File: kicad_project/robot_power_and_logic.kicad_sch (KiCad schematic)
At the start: 16 parts

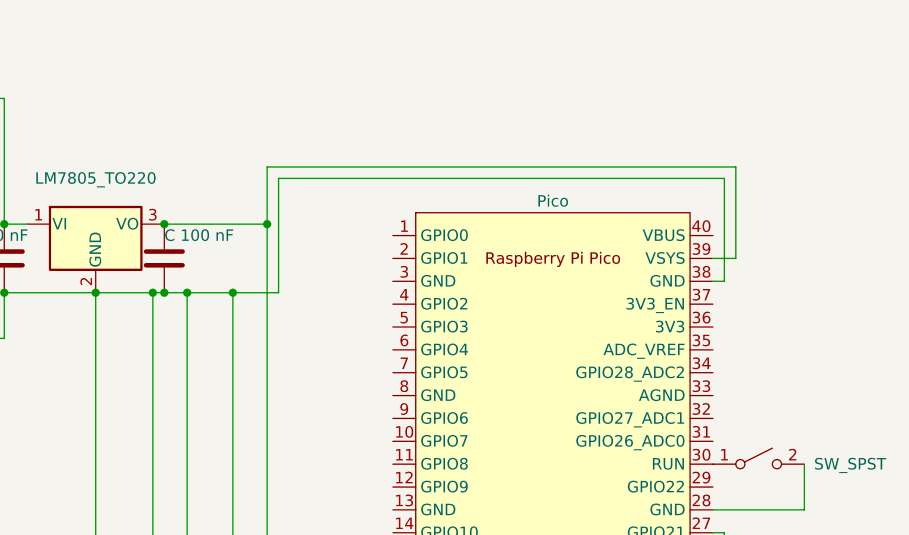
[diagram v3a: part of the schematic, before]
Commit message: Add HC-05 pinout
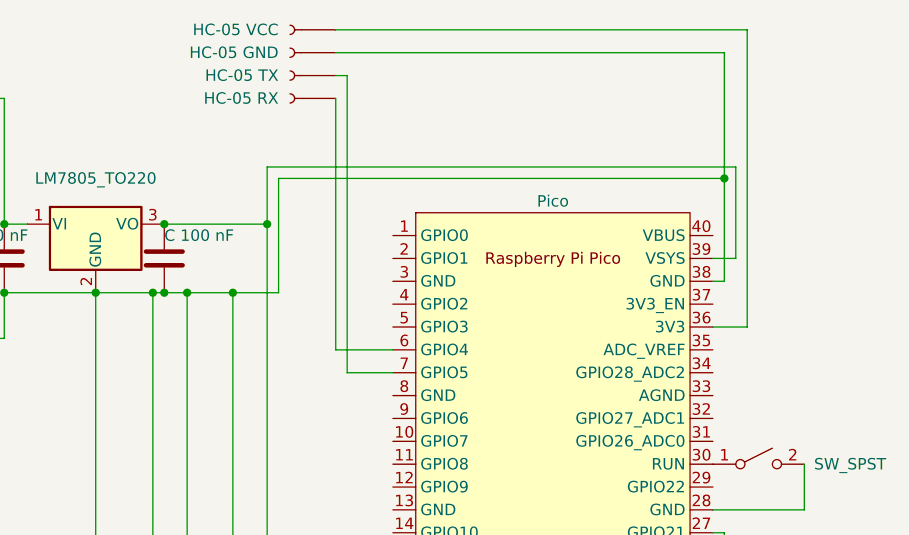
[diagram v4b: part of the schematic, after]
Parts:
- added J?: HC-05 RX, symbol Connector:Conn_01x01_Female
- added J?: HC-05 GND, symbol Connector:Conn_01x01_Female
- added J?: HC-05 VCC, symbol Connector:Conn_01x01_Female
- added J?: HC-05 TX, symbol Connector:Conn_01x01_Female
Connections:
- net at BT?.2 (-), C?.1, C?.1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: now also J?.1 (Pin_1)
- net at U?.36 (3V3): now also J?.1 (Pin_1)
- net at U?.6 (GPIO4): now also J?.1 (Pin_1)
- net at U?.7 (GPIO5): now also J?.1 (Pin_1)
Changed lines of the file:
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@@
   (junction (at 113.03 165.1) (diameter 0) (color 0 0 0 0)
   )
+  (junction (at 139.7 40.64) (diameter 0) (color 0 0 0 0)
+  )
   (junction (at 77.47 45.72) (diameter 0) (color 0 0 0 0)
   )
@@
     (stroke (width 0) (type default) (color 0 0 0 0))
   )
+  (wire (pts (xy 96.52 26.67) (xy 139.7 26.67))
+    (stroke (width 0) (type default) (color 0 0 0 0))
+  )
   (wire (pts (xy 118.11 215.9) (xy 113.03 215.9))
     (stroke (width 0) (type default) (color 0 0 0 0))
@@
     (stroke (width 0) (type default) (color 0 0 0 0))
   )
+  (wire (pts (xy 142.24 57.15) (xy 138.43 57.15))
+    (stroke (width 0) (type default) (color 0 0 0 0))
+  )
   (wire (pts (xy 113.03 215.9) (xy 110.49 215.9))
     (stroke (width 0) (type default) (color 0 0 0 0))
@@
     (stroke (width 0) (type default) (color 0 0 0 0))
   )
+  (wire (pts (xy 139.7 26.67) (xy 139.7 40.64))
+    (stroke (width 0) (type default) (color 0 0 0 0))
+  )
   (wire (pts (xy 59.69 45.72) (xy 62.23 45.72))
     (stroke (width 0) (type default) (color 0 0 0 0))
@@
     (stroke (width 0) (type default) (color 0 0 0 0))
   )
+  (wire (pts (xy 142.24 24.13) (xy 142.24 57.15))
+    (stroke (width 0) (type default) (color 0 0 0 0))
+  )
   (wire (pts (xy 139.7 157.48) (xy 101.6 157.48))
     (stroke (width 0) (type default) (color 0 0 0 0))
@@
     (stroke (width 0) (type default) (color 0 0 0 0))
   )
+  (wire (pts (xy 97.79 29.21) (xy 96.52 29.21))
+    (stroke (width 0) (type default) (color 0 0 0 0))
+  )
   (wire (pts (xy 120.65 215.9) (xy 118.11 215.9))
     (stroke (width 0) (type default) (color 0 0 0 0))
@@
     (stroke (width 0) (type default) (color 0 0 0 0))
   )
+  (wire (pts (xy 97.79 62.23) (xy 97.79 29.21))
+    (stroke (width 0) (type default) (color 0 0 0 0))
+  )
   (wire (pts (xy 110.49 214.63) (xy 110.49 215.9))
     (stroke (width 0) (type default) (color 0 0 0 0))
@@
     (stroke (width 0) (type default) (color 0 0 0 0))
   )
+  (wire (pts (xy 96.52 59.69) (xy 96.52 31.75))
+    (stroke (width 0) (type default) (color 0 0 0 0))
+  )
   (wire (pts (xy 128.27 124.46) (xy 152.4 124.46))
     (stroke (width 0) (type default) (color 0 0 0 0))
@@
     (stroke (width 0) (type default) (color 0 0 0 0))
   )
+  (wire (pts (xy 102.87 62.23) (xy 97.79 62.23))
+    (stroke (width 0) (type default) (color 0 0 0 0))
+  )
   (wire (pts (xy 120.65 214.63) (xy 120.65 215.9))
     (stroke (width 0) (type default) (color 0 0 0 0))
   )
+  (wire (pts (xy 96.52 24.13) (xy 142.24 24.13))
+    (stroke (width 0) (type default) (color 0 0 0 0))
+  )
   (wire (pts (xy 140.97 49.53) (xy 140.97 39.37))
     (stroke (width 0) (type default) (color 0 0 0 0))
@@
   )
   (wire (pts (xy 80.01 53.34) (xy 77.47 53.34))
+    (stroke (width 0) (type default) (color 0 0 0 0))
+  )
+  (wire (pts (xy 102.87 59.69) (xy 96.52 59.69))
     (stroke (width 0) (type default) (color 0 0 0 0))
   )
@@
     (pin "2")
   )
+  (symbol (lib_id "Connector:Conn_01x01_Female") (at 91.44 31.75 180) (unit 1)
+    (in_bom yes) (on_board yes)
+    (property "Reference" "J?" (id 0) (at 90.17 33.0201 0)
+      (effects (font (size 1.27 1.27)) (justify left) hide)
+    )
+    (property "Value" "HC-05 RX" (id 1) (at 90.17 31.75 0)
+      (effects (font (size 1.27 1.27)) (justify left))
+    )
+    (property "Footprint" "" (id 2) (at 91.44 31.75 0)
+      (effects (font (size 1.27 1.27)) hide)
+    )
+    (property "Datasheet" "~" (id 3) (at 91.44 31.75 0)
+      (effects (font (size 1.27 1.27)) hide)
+    )
+    (pin "1")
+  )
+  (symbol (lib_id "Connector:Conn_01x01_Female") (at 91.44 26.67 180) (unit 1)
+    (in_bom yes) (on_board yes)
+    (property "Reference" "J?" (id 0) (at 90.17 27.9401 0)
+      (effects (font (size 1.27 1.27)) (justify left) hide)
+    )
+    (property "Value" "HC-05 GND" (id 1) (at 90.17 26.67 0)
+      (effects (font (size 1.27 1.27)) (justify left))
+    )
+    (property "Footprint" "" (id 2) (at 91.44 26.67 0)
+      (effects (font (size 1.27 1.27)) hide)
+    )
+    (property "Datasheet" "~" (id 3) (at 91.44 26.67 0)
+      (effects (font (size 1.27 1.27)) hide)
+    )
+    (pin "1")
+  )
   (symbol (lib_id "Regulator_Linear:LM7805_TO220") (at 69.85 45.72 0) (unit 1)
     (in_bom yes) (on_board yes) (fields_autoplaced)
@@
     (pin "1")
     (pin "2")
+  )
+  (symbol (lib_id "Connector:Conn_01x01_Female") (at 91.44 24.13 180) (unit 1)
+    (in_bom yes) (on_board yes)
+    (property "Reference" "J?" (id 0) (at 90.17 25.4001 0)
+      (effects (font (size 1.27 1.27)) (justify left) hide)
+    )
+    (property "Value" "HC-05 VCC" (id 1) (at 90.17 24.13 0)
+      (effects (font (size 1.27 1.27)) (justify left))
+    )
+    (property "Footprint" "" (id 2) (at 91.44 24.13 0)
+      (effects (font (size 1.27 1.27)) hide)
+    )
+    (property "Datasheet" "~" (id 3) (at 91.44 24.13 0)
+      (effects (font (size 1.27 1.27)) hide)
+    )
+    (pin "1")
   )
   (symbol (lib_id "Device:C") (at 77.47 49.53 0) (unit 1)
@@
     (pin "2")
   )
+  (symbol (lib_id "Connector:Conn_01x01_Female") (at 91.44 29.21 180) (unit 1)
+    (in_bom yes) (on_board yes)
+    (property "Reference" "J?" (id 0) (at 90.17 30.4801 0)
+      (effects (font (size 1.27 1.27)) (justify left) hide)
+    )
+    (property "Value" "HC-05 TX" (id 1) (at 90.17 29.21 0)
+      (effects (font (size 1.27 1.27)) (justify left))
+    )
+    (property "Footprint" "" (id 2) (at 91.44 29.21 0)
+      (effects (font (size 1.27 1.27)) hide)
+    )
+    (property "Datasheet" "~" (id 3) (at 91.44 29.21 0)
+      (effects (font (size 1.27 1.27)) hide)
+    )
+    (pin "1")
+  )
   (symbol (lib_id "Device:C") (at 76.2 163.83 180) (unit 1)
     (in_bom yes) (on_board yes)
@@
       (reference "C?") (unit 1) (value "C 100 nF") (footprint "")
     )
+    (path "/7d5859f5-db8f-4872-bdc4-7dfd6ca0ffd2"
+      (reference "J?") (unit 1) (value "HC-05 RX") (footprint "")
+    )
+    (path "/86be7c52-226c-4d66-ac8a-53e16ac5077b"
+      (reference "J?") (unit 1) (value "HC-05 GND") (footprint "")
+    )
+    (path "/bed31f51-5829-4a57-932e-babb8069344e"
+      (reference "J?") (unit 1) (value "HC-05 VCC") (footprint "")
+    )
+    (path "/dfb84b91-445d-4d36-8830-bfb0723ae88f"
+      (reference "J?") (unit 1) (value "HC-05 TX") (footprint "")
+    )
     (path "/a1814adc-4ac2-4263-9209-7cd9c36fb2df"

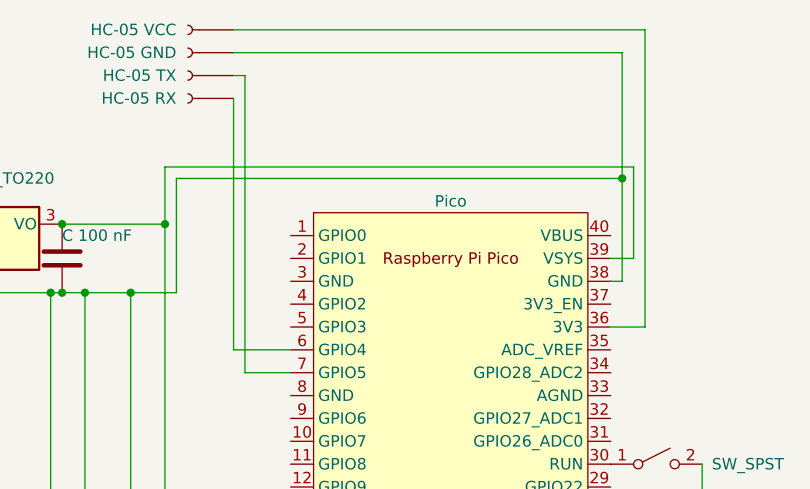
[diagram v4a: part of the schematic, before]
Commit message: Update HC-05 power connection
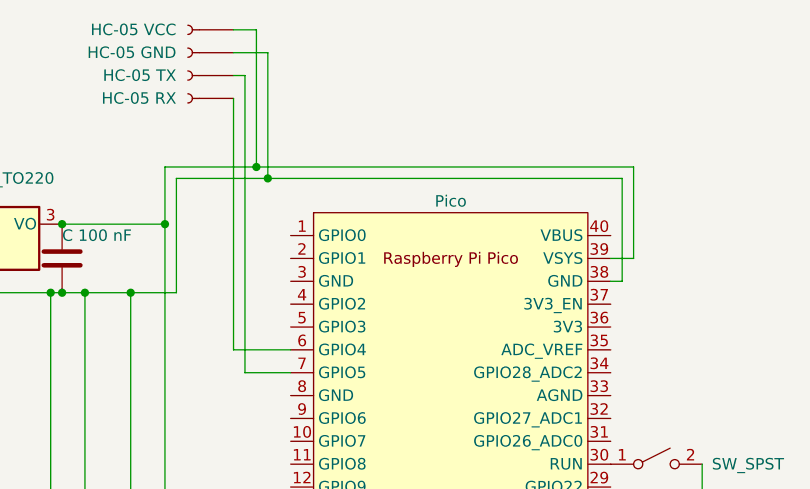
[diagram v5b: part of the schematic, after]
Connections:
- net at C?.1, C?.2, C?.2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: now also J?.1 (Pin_1)
- net at U?.36 (3V3): no longer J?.1 (Pin_1)
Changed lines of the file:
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@@
   (junction (at 110.49 156.21) (diameter 0) (color 0 0 0 0)
   )
+  (junction (at 99.06 39.37) (diameter 0) (color 0 0 0 0)
+  )
   (junction (at 76.2 167.64) (diameter 0) (color 0 0 0 0)
   )
@@
   (junction (at 113.03 165.1) (diameter 0) (color 0 0 0 0)
   )
-  (junction (at 139.7 40.64) (diameter 0) (color 0 0 0 0)
+  (junction (at 100.33 40.64) (diameter 0) (color 0 0 0 0)
   )
   (junction (at 77.47 45.72) (diameter 0) (color 0 0 0 0)
@@
     (stroke (width 0) (type default) (color 0 0 0 0))
   )
+  (wire (pts (xy 100.33 26.67) (xy 100.33 40.64))
+    (stroke (width 0) (type default) (color 0 0 0 0))
+  )
   (wire (pts (xy 120.65 154.94) (xy 120.65 156.21))
     (stroke (width 0) (type default) (color 0 0 0 0))
@@
     (stroke (width 0) (type default) (color 0 0 0 0))
   )
+  (wire (pts (xy 96.52 24.13) (xy 99.06 24.13))
+    (stroke (width 0) (type default) (color 0 0 0 0))
+  )
   (wire (pts (xy 69.85 156.21) (xy 69.85 53.34))
     (stroke (width 0) (type default) (color 0 0 0 0))
@@
     (stroke (width 0) (type default) (color 0 0 0 0))
   )
-  (wire (pts (xy 96.52 26.67) (xy 139.7 26.67))
-    (stroke (width 0) (type default) (color 0 0 0 0))
-  )
   (wire (pts (xy 118.11 215.9) (xy 113.03 215.9))
     (stroke (width 0) (type default) (color 0 0 0 0))
@@
     (stroke (width 0) (type default) (color 0 0 0 0))
   )
-  (wire (pts (xy 142.24 57.15) (xy 138.43 57.15))
-    (stroke (width 0) (type default) (color 0 0 0 0))
-  )
   (wire (pts (xy 113.03 215.9) (xy 110.49 215.9))
     (stroke (width 0) (type default) (color 0 0 0 0))
@@
     (stroke (width 0) (type default) (color 0 0 0 0))
   )
-  (wire (pts (xy 139.7 26.67) (xy 139.7 40.64))
-    (stroke (width 0) (type default) (color 0 0 0 0))
-  )
   (wire (pts (xy 59.69 45.72) (xy 62.23 45.72))
     (stroke (width 0) (type default) (color 0 0 0 0))
@@
     (stroke (width 0) (type default) (color 0 0 0 0))
   )
-  (wire (pts (xy 142.24 24.13) (xy 142.24 57.15))
-    (stroke (width 0) (type default) (color 0 0 0 0))
-  )
   (wire (pts (xy 139.7 157.48) (xy 101.6 157.48))
     (stroke (width 0) (type default) (color 0 0 0 0))
@@
     (stroke (width 0) (type default) (color 0 0 0 0))
   )
+  (wire (pts (xy 139.7 40.64) (xy 139.7 52.07))
+    (stroke (width 0) (type default) (color 0 0 0 0))
+  )
   (wire (pts (xy 97.79 161.29) (xy 97.79 124.46))
     (stroke (width 0) (type default) (color 0 0 0 0))
@@
     (stroke (width 0) (type default) (color 0 0 0 0))
   )
+  (wire (pts (xy 96.52 26.67) (xy 100.33 26.67))
+    (stroke (width 0) (type default) (color 0 0 0 0))
+  )
   (wire (pts (xy 105.41 105.41) (xy 85.09 105.41))
     (stroke (width 0) (type default) (color 0 0 0 0))
@@
     (stroke (width 0) (type default) (color 0 0 0 0))
   )
+  (wire (pts (xy 100.33 40.64) (xy 90.17 40.64))
+    (stroke (width 0) (type default) (color 0 0 0 0))
+  )
   (wire (pts (xy 99.06 119.38) (xy 102.87 119.38))
     (stroke (width 0) (type default) (color 0 0 0 0))
@@
     (stroke (width 0) (type default) (color 0 0 0 0))
   )
-  (wire (pts (xy 139.7 52.07) (xy 139.7 40.64))
-    (stroke (width 0) (type default) (color 0 0 0 0))
-  )
   (wire (pts (xy 96.52 59.69) (xy 96.52 31.75))
     (stroke (width 0) (type default) (color 0 0 0 0))
@@
     (stroke (width 0) (type default) (color 0 0 0 0))
   )
-  (wire (pts (xy 139.7 40.64) (xy 90.17 40.64))
+  (wire (pts (xy 139.7 40.64) (xy 100.33 40.64))
     (stroke (width 0) (type default) (color 0 0 0 0))
   )
@@
     (stroke (width 0) (type default) (color 0 0 0 0))
   )
+  (wire (pts (xy 99.06 39.37) (xy 88.9 39.37))
+    (stroke (width 0) (type default) (color 0 0 0 0))
+  )
   (wire (pts (xy 43.18 58.42) (xy 59.69 58.42))
     (stroke (width 0) (type default) (color 0 0 0 0))
@@
     (stroke (width 0) (type default) (color 0 0 0 0))
   )
-  (wire (pts (xy 96.52 24.13) (xy 142.24 24.13))
-    (stroke (width 0) (type default) (color 0 0 0 0))
-  )
   (wire (pts (xy 140.97 49.53) (xy 140.97 39.37))
     (stroke (width 0) (type default) (color 0 0 0 0))
@@
     (stroke (width 0) (type default) (color 0 0 0 0))
   )
-  (wire (pts (xy 138.43 52.07) (xy 139.7 52.07))
-    (stroke (width 0) (type default) (color 0 0 0 0))
-  )
   (wire (pts (xy 138.43 82.55) (xy 140.97 82.55))
     (stroke (width 0) (type default) (color 0 0 0 0))
   )
-  (wire (pts (xy 140.97 39.37) (xy 88.9 39.37))
-    (stroke (width 0) (type default) (color 0 0 0 0))
-  )
+  (wire (pts (xy 99.06 24.13) (xy 99.06 39.37))
+    (stroke (width 0) (type default) (color 0 0 0 0))
+  )
+  (wire (pts (xy 140.97 39.37) (xy 99.06 39.37))
+    (stroke (width 0) (type default) (color 0 0 0 0))
+  )
+  (wire (pts (xy 139.7 52.07) (xy 138.43 52.07))
+    (stroke (width 0) (type default) (color 0 0 0 0))
+  )
